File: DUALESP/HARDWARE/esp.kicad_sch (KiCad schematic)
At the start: 35 parts, among them J3 ESP_SERIAL_1, J4 ESP_SERIAL_0, J5 VGA, J7 MOUSE, J8 KEYBOARD, J9 AUDIO OUT, U12 74LS244, U13 74HC595, U14 74HC165, U15 ESP32_MODULE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

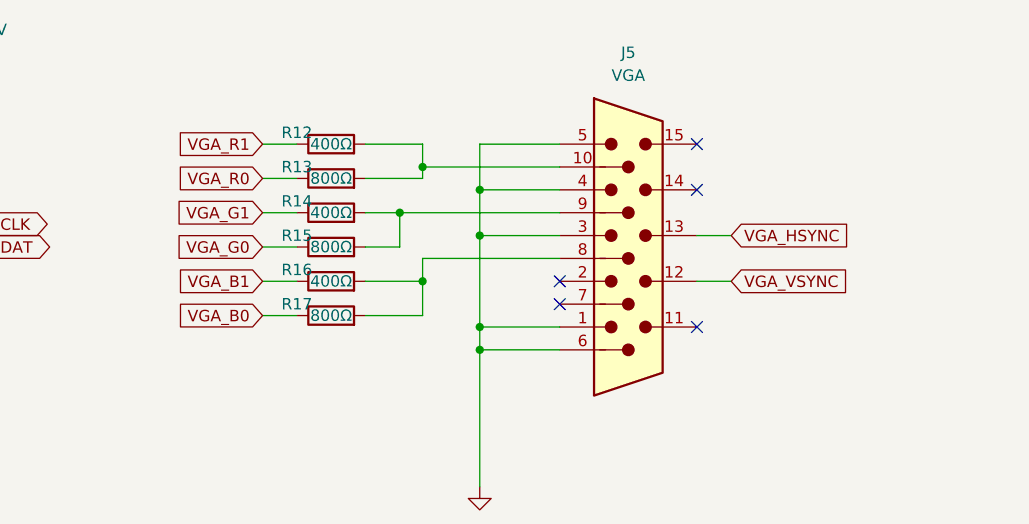
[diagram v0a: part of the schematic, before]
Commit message: fix ESP layout issues
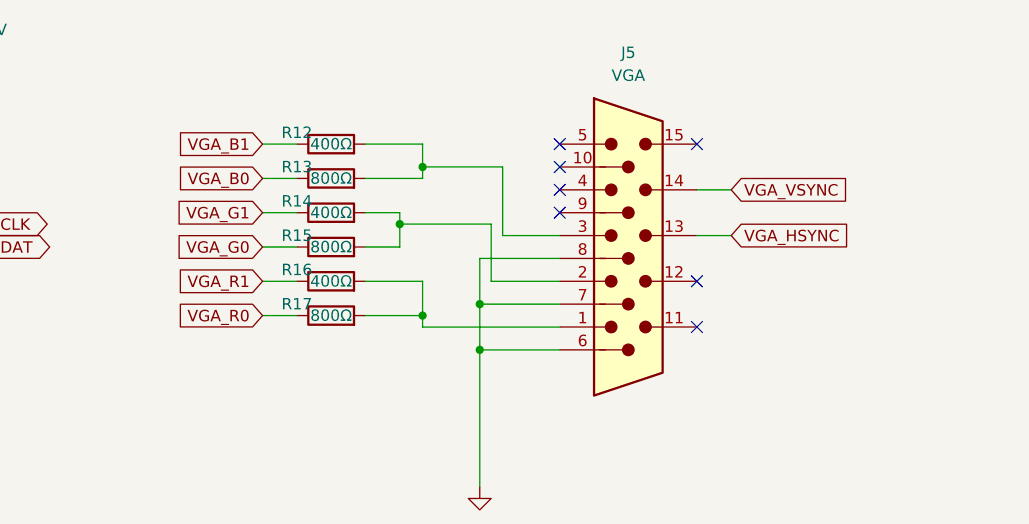
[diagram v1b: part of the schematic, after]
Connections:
- net GND: now also J5.7, J5.8; no longer J5.1, J5.3, J5.4, J5.5
- net VGA_B0: now also R13.1; no longer R17.1
- net VGA_B1: now also R12.1; no longer R16.1
- net VGA_R0: now also R17.1; no longer R13.1
- net VGA_R1: now also R16.1; no longer R12.1
- net VGA_VSYNC: now also J5.14; no longer J5.12
- net at R14.2, R15.2: now also J5.2; no longer J5.9
- net at R12.2, R13.2: now also J5.3; no longer J5.10
- net at R16.2, R17.2: now also J5.1; no longer J5.8
- no-connect marks 30 -> 32

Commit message: ESPIO updates
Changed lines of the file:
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@@
 (kicad_sch
-	(version 20231120)
+	(version 20250114)
 	(generator "eeschema")
-	(generator_version "8.0")
+	(generator_version "9.0")
 	(paper "USLedger")
 	(title_block
 		(title "ISA DUAL ESP32")
-		(date "2025-06-21")
-		(rev "V1.1")
+		(date "2025-06-28")
+		(rev "V1.2")
 	)
 	(junction

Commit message: ESPIO updates
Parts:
- J5: symbol Connector:DE15_Plug_HighDensity -> Connector:DE15_Socket_HighDensity
- U14: value 74HC165 -> 74ACT165
- U5: value 74LS32 -> 74F32
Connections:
- net GND: now also J5.10, J5.5
- net ~{ESP0_RD}: no longer RR2.6 (R5)
- net ~{ESP0_WR}: no longer RR2.4 (R3)
- net ~{ESP1_RD}: no longer RR2.7 (R6)
- net ~{ESP1_WR}: no longer RR2.5 (R4)
- no-connect marks 32 -> 34
